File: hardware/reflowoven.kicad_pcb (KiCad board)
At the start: 2 copper layers, 63.5 x 67.3 mm, 29 parts, among them P1 USB-A-SHLD, P2 CONN_6, P3 CONN_2, P5 CONN_2, U1 FT232RL, U2 255-3100-ND, U3 MSP430G2553IPW20, U4 AD594/95, U5 LM317, X1 CRYSTAL

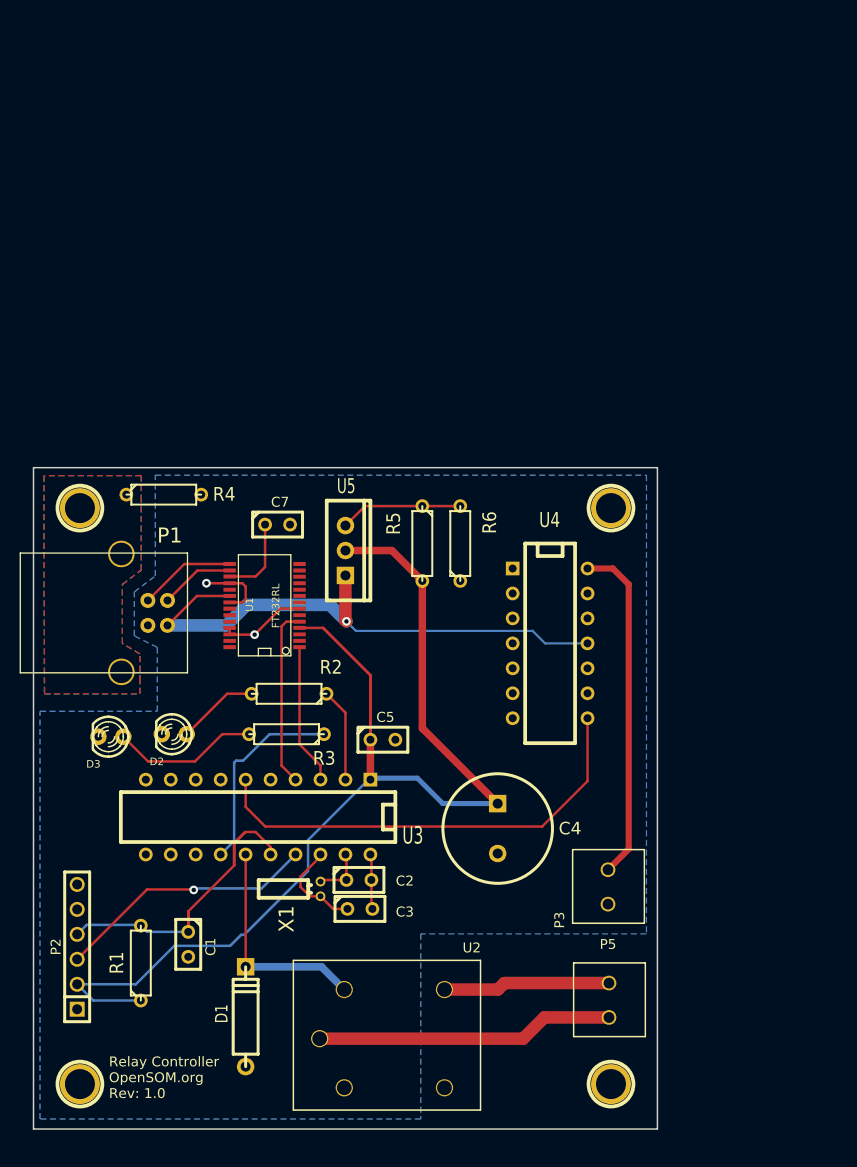
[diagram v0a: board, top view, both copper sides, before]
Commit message: First round of changes to add additional relays and thermal couples
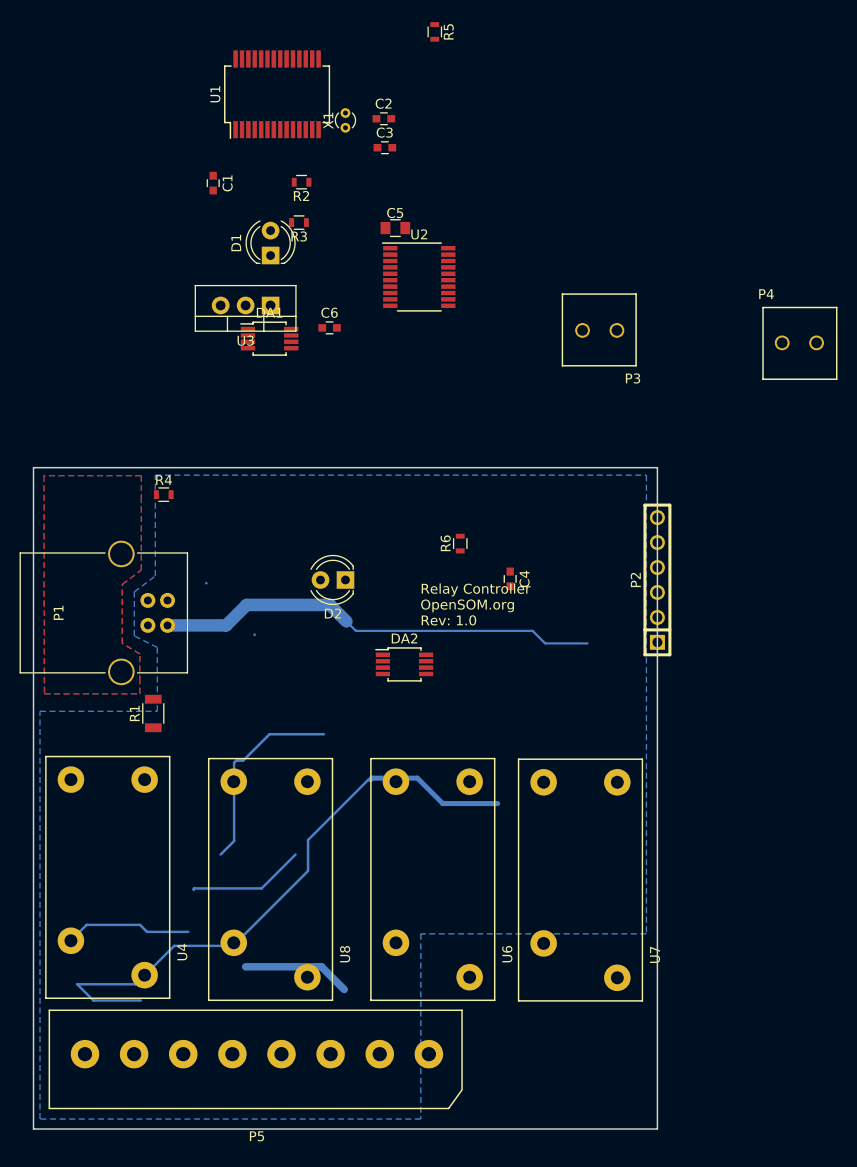
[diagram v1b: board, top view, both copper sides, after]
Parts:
- removed 1PIN (x4): P***, 1pin
- removed C7: 100nF, C1
- removed D3: LED, LED-3MM
- removed U5: LM317, TO220_VERT
- added C6: 100nF, Capacitors_SMD:C_0603, F.Cu at (158.4, 133.1)
- added DA1: AD8495, Housings_SSOP:MSOP-8_3x3mm_Pitch0.65mm, F.Cu at (152.3, 134.2)
- added DA2: AD8495, Housings_SSOP:MSOP-8_3x3mm_Pitch0.65mm, F.Cu at (166.0, 167.3)
- added P4: CONN_2, svolpe-custom-mod:1751248, F.Cu at (206.2, 134.6)
- added U6: MCHRM3H, svolpe-custom-mod:MCHRM3H, F.Cu at (168.9, 189.2)
- added U7: MCHRM3H, svolpe-custom-mod:MCHRM3H, F.Cu at (183.9, 189.3)
- added U8: MCHRM3H, svolpe-custom-mod:MCHRM3H, F.Cu at (152.4, 189.2)
- C1: value 1nF -> 100nF; footprint C1 -> Capacitors_SMD:C_0603
- C2: value 12pF -> 1nF; footprint C1 -> Capacitors_SMD:C_0603
- C3: footprint C1 -> Capacitors_SMD:C_0603
- C4: value 10uF -> 12pF; footprint C2V10 -> Capacitors_SMD:C_0603
- C5: value 100nF -> 10uF; footprint C1 -> Capacitors_SMD:C_0805
- D1: value DIODE -> LED; footprint D4 -> LEDs:LED_D4.0mm
- D2: footprint LED-3MM -> LEDs:LED_D4.0mm
- P1: footprint USB_B_WSHIELD -> Connectors:USB_B
- P3: footprint term-2 -> svolpe-custom-mod:1751248
- P5: value CONN_2 -> CONN_01X08; footprint term-2 -> svolpe-custom-mod:1935226
- R1: value 47K -> 0; footprint R3 -> Resistors_SMD:R_1206
- R2, R3: footprint R3 -> Resistors_SMD:R_0603
- R4: value 0 -> 47K; footprint R3 -> Resistors_SMD:R_0603
- R5: value 0 -> 330; footprint R3 -> Resistors_SMD:R_0603
- R6: value 0 -> 560; footprint R3 -> Resistors_SMD:R_0603
- U1: footprint SSOP28 -> Housings_SSOP:SSOP-28_5.3x10.2mm_Pitch0.65mm
- U2: value 255-3100-ND -> MSP430G2553IPW20; footprint 255-3100-ND -> Housings_SSOP:TSSOP-20_4.4x6.5mm_Pitch0.65mm
- U3: value MSP430G2553IPW20 -> LM317; footprint DIP-20__300 -> TO_SOT_Packages_THT:TO-220_Vertical
- U4: value AD594/95 -> MCHRM3H; footprint DIP-14__300 -> svolpe-custom-mod:MCHRM3H
- X1: footprint Crystal_Round_Horizontal_2mm_RevA_25Apr2012 -> Crystals:Crystal_Round_d1.0mm_Vertical
- moved C3 77.5 mm to (164.0, 114.8)
- moved C1 77.5 mm to (146.6, 118.4)
- moved C2 77.5 mm to (163.9, 111.8)
- moved U2 77.5 mm to (167.5, 127.9)
- moved X1 77.5 mm to (160.0, 112.7)
- moved D1 77.5 mm to (152.4, 125.7)
- moved P2 69.9 mm to (191.8, 158.8)
- moved P3 56.6 mm to (185.9, 133.3), turned to 180 degrees
- moved R2 52.1 mm to (155.5, 118.3)
- moved R3 52.1 mm to (155.3, 122.4)
- moved U1 52.1 mm to (153.1, 109.3)
- moved C5 52.1 mm to (165.1, 122.9)
- moved R5 52.1 mm to (169.1, 103.0)
- moved U3 52.1 mm to (152.4, 130.8)
- moved U4 50.9 mm to (135.8, 189.0)
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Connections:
- C1 pad 1: /TCK -> Net-(C1-Pad1)
- C2 pad 1: /XIN -> /TDIO
- C3 pad 1: /XOUT -> /XIN
- C4 pad 1: +3.3V -> /XOUT
- C5 pad 1: +3.3V -> Net-(C5-Pad1)
- C5 pad 2: GND -> Net-(C5-Pad2)
- D1 pad 1: GND -> Net-(D1-Pad1)
- D1 pad 2: /relay -> GND
- D2 pad 1: N-0000049 -> Net-(D2-Pad1)
- P2 pad 1: (no net) -> Net-(P2-Pad1)
- P2 pad 3: /TDIO -> /TCK
- P2 pad 4: /TCK -> /TDIO
- P2 pad 6: (no net) -> Net-(P2-Pad6)
- P3 pad 1: GND -> /THERMOCOUPLE_1+
- P3 pad 2: /THERMOCOUPLE- -> /THERMOCOUPLE_1-
- P5 pad 1: N-0000045 -> Net-(P5-Pad1)
- P5 pad 2: N-0000044 -> Net-(P5-Pad2)
- R1 pad 1: +3.3V -> /ESD_RING
- R1 pad 2: /TCK -> GND
- R2 pad 2: N-0000049 -> Net-(D1-Pad1)
- R3 pad 2: N-0000052 -> Net-(D2-Pad1)
- R4 pad 1: /ESD_RING -> +3.3V
- R4 pad 2: GND -> /TDIO
- R5 pad 1: N-0000041 -> Net-(R5-Pad1)
- R6 pad 2: N-0000041 -> Net-(R5-Pad1)
- U1 pad 10: (no net) -> Net-(U1-Pad10)
- U1 pad 11: (no net) -> Net-(U1-Pad11)
- U1 pad 12: (no net) -> Net-(U1-Pad12)
- U1 pad 13: (no net) -> Net-(U1-Pad13)
- U1 pad 14: (no net) -> Net-(U1-Pad14)
- U1 pad 17: N-0000042 -> Net-(C1-Pad1)
- U1 pad 19: (no net) -> Net-(U1-Pad19)
- U1 pad 2: (no net) -> Net-(U1-Pad2)
- U1 pad 22: (no net) -> Net-(U1-Pad22)
- U1 pad 23: (no net) -> Net-(U1-Pad23)
- U1 pad 27: (no net) -> Net-(U1-Pad27)
- U1 pad 28: (no net) -> Net-(U1-Pad28)
- U1 pad 3: (no net) -> Net-(U1-Pad3)
- U1 pad 6: (no net) -> Net-(U1-Pad6)
- U1 pad 9: (no net) -> Net-(U1-Pad9)
- U2 pad 1: /relay -> +3.3V
- U2 pad 2: GND -> /P1.0
- U3 pad 1: +3.3V -> /VBUS
- U3 pad 2: /P1.0 -> Net-(R5-Pad1)
- U3 pad 3: /RX -> +3.3V
- U4 pad 1: GND -> Net-(U4-Pad1)
- U4 pad 2: (no net) -> GND
- U4 pad 3: (no net) -> Net-(U4-Pad3)
- U4 pad 4: GND -> Net-(U4-Pad4)
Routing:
- net +3.3V: track 129.7 -> 0.00 mm
- net /TEMP: track 46.7 -> 0.00 mm
- net (no net): track 0.00 -> 43.2 mm
- net Net-(U8-Pad4): track 0.00 -> 42.9 mm
- net /THERMOCOUPLE-: track 34.8 -> 0.00 mm
- net /TCK: track 34.5 -> 0.00 mm
- net N-0000045: track 30.3 -> 0.00 mm
- net /TDIO: track 26.7 -> 0.00 mm, vias 1 -> 0
- net /relay: track 22.4 -> 0.00 mm
- net GND: track 21.7 -> 0.00 mm, vias 2 -> 0
- net /P1.6: track 20.3 -> 0.00 mm
- net Net-(U4-Pad3): track 0.00 -> 18.7 mm
- net /TX: track 18.2 -> 0.00 mm
- net N-0000044: track 17.0 -> 0.00 mm
- net N-0000052: track 15.0 -> 0.00 mm
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
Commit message: Finalized layout with 2 thermocouples and 4 relays
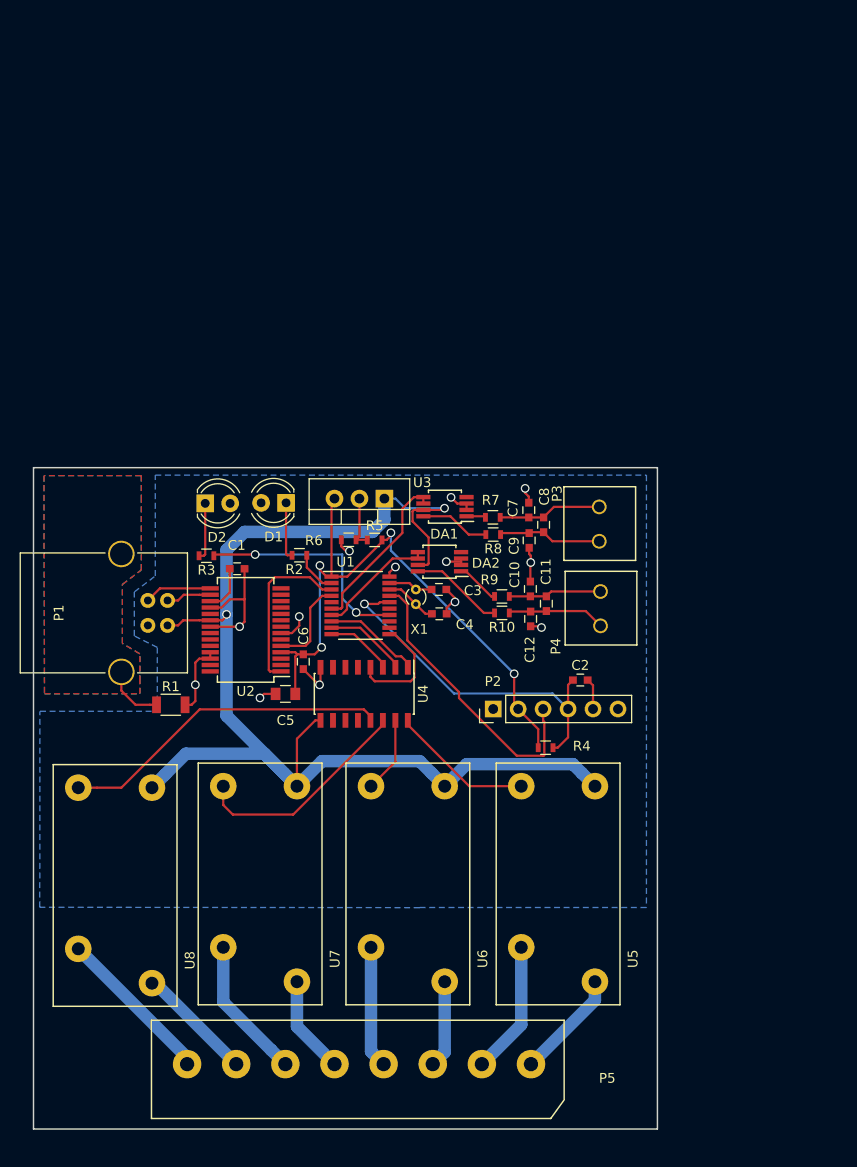
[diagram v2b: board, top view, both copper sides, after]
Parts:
- added C10: 10nF, Capacitors_SMD:C_0603, F.Cu at (178.8, 159.7)
- added C11: 100nF, Capacitors_SMD:C_0603, F.Cu at (180.5, 161.2)
- added C12: 10nF, Capacitors_SMD:C_0603, F.Cu at (178.9, 162.7)
- added C7: 10nF, Capacitors_SMD:C_0603, F.Cu at (178.7, 151.6)
- added C8: 100nF, Capacitors_SMD:C_0603, F.Cu at (180.2, 153.1)
- added C9: 10nF, Capacitors_SMD:C_0603, F.Cu at (178.7, 154.7)
- added R10: 10K, Resistors_SMD:R_0603, F.Cu at (175.9, 162.1)
- added R7: 10K, Resistors_SMD:R_0603, F.Cu at (175.0, 152.4)
- added R8: 10K, Resistors_SMD:R_0603, F.Cu at (175.1, 154.1)
- added R9: 10K, Resistors_SMD:R_0603, F.Cu at (175.9, 160.4)
- added U5: MCHRM3H, svolpe-custom-mod:MCHRM3H, F.Cu at (181.7, 189.7)
- P2: footprint PIN_ARRAY-6X1 -> Pin_Headers:Pin_Header_Straight_1x06_Pitch2.54mm
- U1: value FT232RL -> MSP430G2553IPW20; footprint Housings_SSOP:SSOP-28_5.3x10.2mm_Pitch0.65mm -> Housings_SSOP:TSSOP-20_4.4x6.5mm_Pitch0.65mm
- U2: value MSP430G2553IPW20 -> FT232RL; footprint Housings_SSOP:TSSOP-20_4.4x6.5mm_Pitch0.65mm -> Housings_SSOP:SSOP-28_5.3x10.2mm_Pitch0.65mm
- U4: value MCHRM3H -> ULN2003A; footprint svolpe-custom-mod:MCHRM3H -> Housings_SOIC:SOIC-16_3.9x9.9mm_Pitch1.27mm
- moved C2 60.5 mm to (183.9, 168.9)
- moved U1 52.7 mm to (161.5, 161.3), turned to 0 degrees
- moved R5 52.1 mm to (163.0, 154.7), turned to 0 degrees
- moved X1 49.0 mm to (167.2, 161.2)
- moved C5 48.7 mm to (153.9, 170.3), turned to 180 degrees
- moved R4 46.6 mm to (180.4, 175.8)
- moved C3 45.3 mm to (169.5, 159.7)
- moved U2 40.0 mm to (149.9, 163.8), turned to 180 degrees
- moved C1 39.3 mm to (149.0, 157.6), turned to 0 degrees
- moved R2 38.0 mm to (155.3, 156.2)
- moved R3 35.2 mm to (145.9, 156.3)
- moved C6 34.1 mm to (155.7, 167.1), turned to 270 degrees
- moved P4 33.8 mm to (186.0, 161.7), turned to 90 degrees
- moved U7 32.6 mm to (151.3, 189.7)
- moved U4 32.1 mm to (161.9, 170.3)
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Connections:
- net /TEMP renamed Net-(U2-Pad6)
- C5 pad 1: Net-(C5-Pad1) -> +3.3V
- C5 pad 2: Net-(C5-Pad2) -> GND
- DA1 pad 1: /THERMOCOUPLE_1- -> Net-(DA1-Pad1)
- DA1 pad 2: Net-(DA1-Pad2) -> GND
- DA1 pad 3: Net-(DA1-Pad3) -> GND
- DA1 pad 5: Net-(DA1-Pad5) -> /TEMP_1
- DA1 pad 6: Net-(DA1-Pad6) -> /TEMP_1
- DA1 pad 7: Net-(DA1-Pad7) -> +5V
- DA1 pad 8: /THERMOCOUPLE_1+ -> Net-(DA1-Pad8)
- DA2 pad 1: /THERMOCOUPLE_2- -> Net-(DA2-Pad1)
- DA2 pad 2: Net-(DA2-Pad2) -> GND
- DA2 pad 3: Net-(DA2-Pad3) -> GND
- DA2 pad 5: Net-(DA2-Pad5) -> /TEMP_2
- DA2 pad 6: Net-(DA2-Pad6) -> /TEMP_2
- DA2 pad 7: Net-(DA2-Pad7) -> +5V
- DA2 pad 8: /THERMOCOUPLE_2+ -> Net-(DA2-Pad8)
- P1 pad 1: /VBUS -> +5V
- P3 pad 1: /THERMOCOUPLE_1+ -> /Relays and Themocouples/Thermocouple_1+
- P3 pad 2: /THERMOCOUPLE_1- -> /Relays and Themocouples/Thermocouple_1-
- P4 pad 1: /THERMOCOUPLE_2+ -> /Relays and Themocouples/Thermocouple_2+
- P4 pad 2: /THERMOCOUPLE_2- -> /Relays and Themocouples/Thermocouple_2-
- P5 pad 1: Net-(P5-Pad1) -> /Relays and Themocouples/Relay_1_Term_A
- P5 pad 2: Net-(P5-Pad2) -> /Relays and Themocouples/Relay_1_Term_B
- P5 pad 3: Net-(P5-Pad3) -> /Relays and Themocouples/Relay_2_Term_A
- P5 pad 4: Net-(P5-Pad4) -> /Relays and Themocouples/Relay_2_Term_B
- P5 pad 5: Net-(P5-Pad5) -> /Relays and Themocouples/Relay_3_Term_A
- P5 pad 6: Net-(P5-Pad6) -> /Relays and Themocouples/Relay_3_Term_B
- P5 pad 7: Net-(P5-Pad7) -> /Relays and Themocouples/Relay_4_Term_A
- P5 pad 8: Net-(P5-Pad8) -> /Relays and Themocouples/Relay_4_Term_B
- U1 pad 1: /RX -> +3.3V
- U1 pad 10: Net-(U1-Pad10) -> /Relays and Themocouples/RelayCTRL_3
- U1 pad 11: Net-(U1-Pad11) -> /Relays and Themocouples/RelayCTRL_4
- U1 pad 14: Net-(U1-Pad14) -> /P1.6
- U1 pad 15: /USB_DP -> /relay
- U1 pad 16: /USB_DM -> /TDIO
- U1 pad 17: Net-(C1-Pad1) -> /TCK
- U1 pad 18: GND -> /XOUT
- U1 pad 19: Net-(U1-Pad19) -> /XIN
- U1 pad 2: Net-(U1-Pad2) -> /P1.0
- U1 pad 20: /VBUS -> GND
- U1 pad 3: Net-(U1-Pad3) -> /RX
- U1 pad 4: +3.3V -> /TX
- U1 pad 5: /TX -> Net-(U1-Pad5)
- U1 pad 6: Net-(U1-Pad6) -> /TEMP_1
- U1 pad 7: GND -> /TEMP_2
- U1 pad 8: (no net) -> /Relays and Themocouples/RelayCTRL_1
- U1 pad 9: Net-(U1-Pad9) -> /Relays and Themocouples/RelayCTRL_2
- U2 pad 1: +3.3V -> /RX
- U2 pad 14: /P1.6 -> Net-(U2-Pad14)
- U2 pad 15: /relay -> /USB_DP
- U2 pad 16: /TDIO -> /USB_DM
- U2 pad 17: /TCK -> Net-(C1-Pad1)
- U2 pad 18: /XOUT -> GND
- U2 pad 19: /XIN -> Net-(U2-Pad19)
- U2 pad 2: /P1.0 -> Net-(U2-Pad2)
- U2 pad 20: GND -> +5V
- U2 pad 3: /RX -> Net-(U2-Pad3)
- U2 pad 4: /TX -> +3.3V
- U2 pad 5: Net-(U2-Pad5) -> /TX
- U2 pad 7: Net-(U2-Pad7) -> GND
- U2 pad 8: Net-(U2-Pad8) -> (no net)
- U3 pad 1: /VBUS -> +5V
- U4 pad 1: Net-(U4-Pad1) -> /Relays and Themocouples/RelayCTRL_1
- U4 pad 2: GND -> /Relays and Themocouples/RelayCTRL_2
- U4 pad 3: Net-(U4-Pad3) -> /Relays and Themocouples/RelayCTRL_3
- U4 pad 4: Net-(U4-Pad4) -> /Relays and Themocouples/RelayCTRL_4
- U6 pad 1: Net-(U5-Pad15) -> +5V
- U6 pad 2: GND -> Net-(U4-Pad15)
- U6 pad 3: Net-(U6-Pad3) -> /Relays and Themocouples/Relay_2_Term_A
- U6 pad 4: Net-(U6-Pad4) -> /Relays and Themocouples/Relay_2_Term_B
- U7 pad 1: Net-(U5-Pad14) -> +5V
- U7 pad 2: GND -> Net-(U4-Pad14)
- U7 pad 3: Net-(U7-Pad3) -> /Relays and Themocouples/Relay_3_Term_A
- U7 pad 4: Net-(U7-Pad4) -> /Relays and Themocouples/Relay_3_Term_B
- U8 pad 1: Net-(U5-Pad13) -> +5V
- U8 pad 2: GND -> Net-(U4-Pad13)
- U8 pad 3: Net-(U8-Pad3) -> /Relays and Themocouples/Relay_4_Term_A
- U8 pad 4: Net-(U8-Pad4) -> /Relays and Themocouples/Relay_4_Term_B
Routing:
- net +5V: track 0.00 -> 130.0 mm, vias 0 -> 2
- net +3.3V: track 0.00 -> 63.3 mm, vias 0 -> 4
- net GND: track 0.00 -> 50.0 mm, vias 0 -> 13
- net /VBUS: track 45.2 -> 0.00 mm
- net (no net): track 43.2 -> 0.00 mm
- net Net-(U8-Pad4): track 42.9 -> 0.00 mm
- net /TDIO: track 0.00 -> 35.9 mm, vias 0 -> 1
- net Net-(U4-Pad13): track 0.00 -> 33.8 mm
- net /TCK: track 0.00 -> 29.8 mm
- net /P1.6: track 0.00 -> 23.1 mm, vias 0 -> 2
- net Net-(U4-Pad14): track 0.00 -> 22.8 mm
- net Net-(U4-Pad3): track 18.7 -> 0.00 mm
- net /RX: track 0.00 -> 17.3 mm
- net /TEMP_1: track 0.00 -> 17.0 mm
- net /Relays and Themocouples/Relay_4_Term_B: track 0.00 -> 16.3 mm
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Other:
- rule trace_min: 0.2159 -> 0.01778
- board text removed: "Relay Controller OpenSOM.org Rev: 1.0"

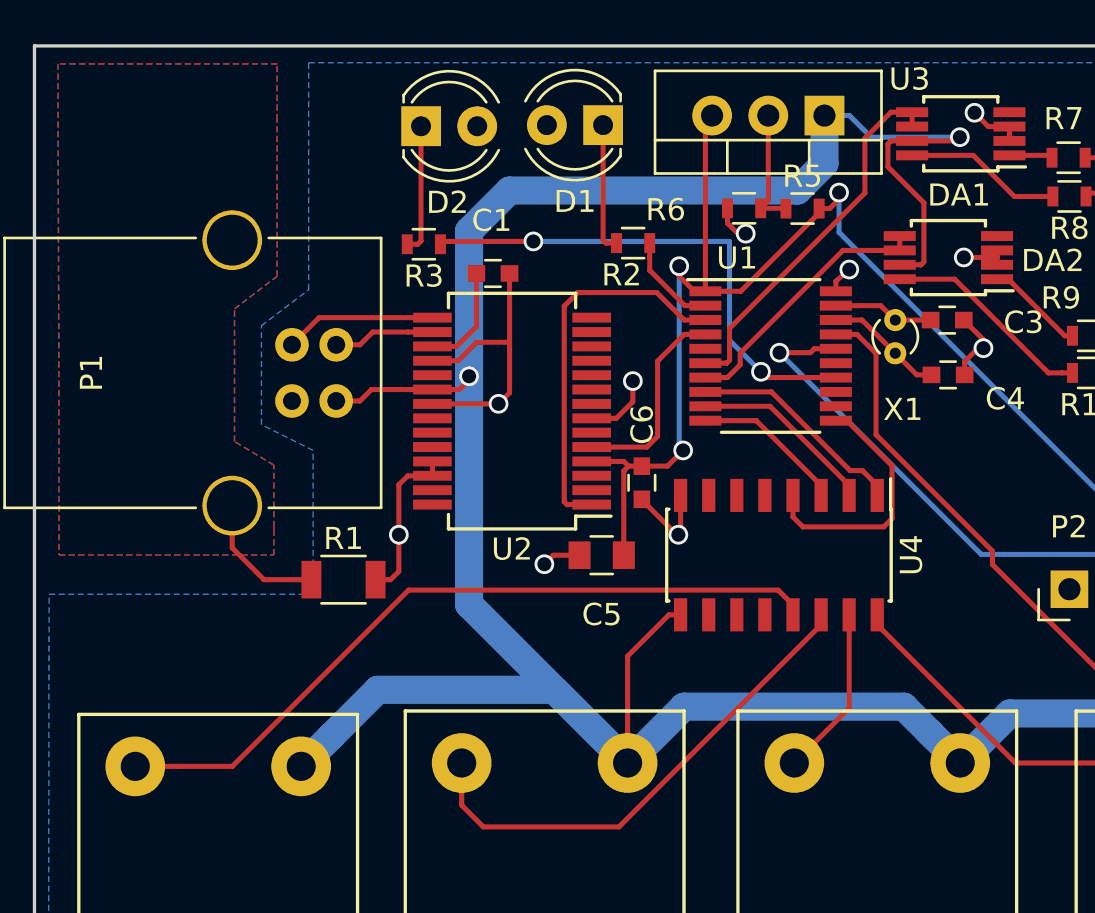
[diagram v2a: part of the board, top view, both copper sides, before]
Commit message: Fixed wireing of LM317 - schematic footprint pinout was incorrect
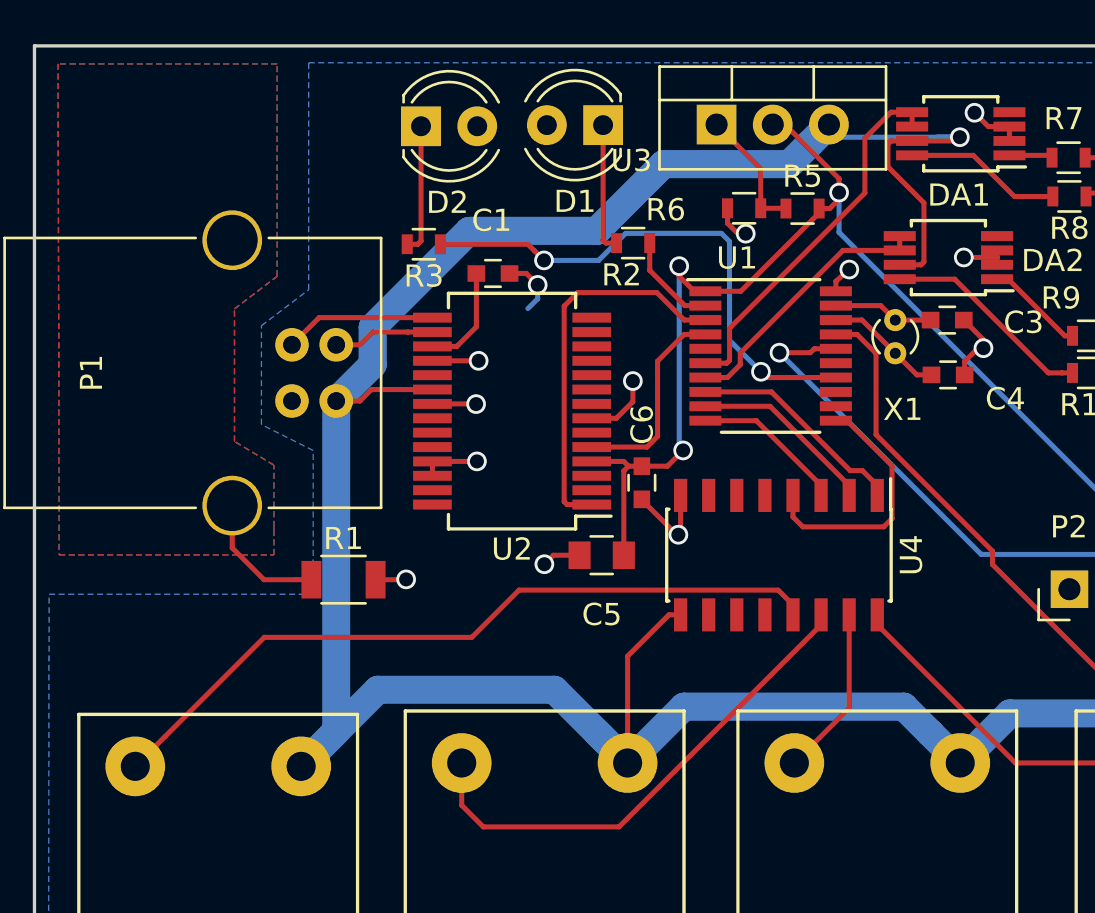
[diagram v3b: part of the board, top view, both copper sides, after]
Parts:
- R5: value 330 -> 750
- R6: value 560 -> 2K
- moved U3 4.89 mm to (159.1, 150.9), turned to 0 degrees
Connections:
- net /relay renamed Net-(U1-Pad15)
- U3 pad 1: +5V -> Net-(R5-Pad1)
- U3 pad 2: Net-(R5-Pad1) -> +3.3V
- U3 pad 3: +3.3V -> +5V
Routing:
- net GND: track 50.0 -> 40.9 mm, vias 13 -> 16
- net +3.3V: track 63.3 -> 60.1 mm
- net /P1.6: track 23.1 -> 24.0 mm
- net +5V: track 130.0 -> 129.7 mm, vias 2 -> 1

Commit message: Change thermocouple circuitry from 5V to 3.3V
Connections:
- C5 pad 1: +3.3V -> +3V3
- C6 pad 1: +3.3V -> +3V3
- DA1 pad 7: +5V -> +3V3
- DA2 pad 7: +5V -> +3V3
- P2 pad 2: +3.3V -> +3V3
- R4 pad 1: +3.3V -> +3V3
- R5 pad 2: +3.3V -> +3V3
- U1 pad 1: +3.3V -> +3V3
- U2 pad 4: +3.3V -> +3V3
- U3 pad 2: +3.3V -> +3V3
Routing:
- net +3V3: track 0.00 -> 80.6 mm, vias 0 -> 5
- net +3.3V: track 60.1 -> 0.00 mm, vias 4 -> 0
- net +5V: track 129.7 -> 112.7 mm, vias 1 -> 0
